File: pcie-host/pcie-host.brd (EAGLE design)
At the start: 167.6 x 111.2 mm, 237 parts, among them Q1 BSH103, Q2 BSH103, Q3 NDS351AN, Q4 NDS351AN, Q5 NDS351AN, U100 UEI15-050-Q12P-C, U104 ISO7240M, U105 ISO7240M, U106 ISO7240M, U107 ISO7240M

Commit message: Initial PCIe host layout complete.
- Needs verification before fabrication.
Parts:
- removed 10K, 30.1K: 9.53k, jonnew:0603
- removed 13.3K: 30.1k, jonnew:0603
- removed C41: 100uF, jonnew:153CLV-0807
- removed C43: 22uF, jonnew:1210-POL
- removed C71: 0.1uF, jonnew:0402
- removed C99: 100nF, RHD2000_eval_board:0603
- removed DI0, DO0: SMA002, jonnew:SMA_JACK_CONREVSMA002-G
- removed TP15: +5V0, jonnew:TESTPOINT_0.035IN
- removed TP_DI0, TP_DI1: MISO1, jonnew:TP09SQ
- removed U$14: FMC_LPC_160_PIN, jonnew:FMC_LPC_MALE_WITH_SP601_BSILK
- removed U$15, U$8: SCREW4, jonnew:SCREW4
- added DI2, DO2: SMA002, jonnew:SMA_JACK_CONREVSMA002-G
- added FMC_LPC: FMC_LPC_160_PIN, jonnew:FMC_LPC_MALE_WITH_SP601_BSILK
- added R13: 4.7k, cyclops:0603
- added R29: 100, jonnew:0603
- added R37: 22, jonnew:0402
- added TP11: +3.3V, jonnew:TESTPOINT_0.035IN
- added TP12: +12V(FPGA), jonnew:TESTPOINT_0.035IN
- added TP5: PASS, jonnew:TP06R
- added TP9: VPROTECT(+4.3V), jonnew:TESTPOINT_0.035IN
- added U1: ISO, jonnew:SCREW4
- added U18: COMM, jonnew:SCREW4
- C1: value 0.1uF -> 1uF
- C10: value (none) -> 10nF
- C11: value (none) -> 0.01uF
- C12: value (none) -> 47nF
- C13: value 0.1uF -> 4.7uF; device jonnew:0603 -> jonnew:0805
- C14: value 10uF -> 0.1uF; device jonnew:1206 -> jonnew:0402
- C15, C16, C35: device RHD2000_eval_board:0603 -> jonnew:0402
- C17, C5, C55: device RHD2000_eval_board:0603 -> jonnew:0603
- C18: value 0.1uF -> 4.7uF; device RHD2000_eval_board:0603 -> jonnew:1206
- C19: value 22uF -> 4.7F; device jonnew:1210-POL -> jonnew:1206
- C20: value (none) -> 1uF; device jonnew:0402 -> jonnew:0805
- C21, C24: value (none) -> 22uF; device jonnew:0402 -> jonnew:1206
- C22: value (none) -> 4.7uF; device jonnew:0402 -> jonnew:1206
- C23: value (none) -> 0.1uF
- C25: value 100nF -> 0.1uF; device jonnew:0603 -> RHD2000_eval_board:0603
- C26: value 1uF -> 0.01uF; device RHD2000_eval_board:0603 -> jonnew:0402
- C27: value 22uF -> 10nF; device jonnew:1210-POL -> jonnew:0402
- C28: value 4.7uF -> 10nF; device jonnew:0805 -> jonnew:0402
- C29: value 100nF -> 0.1uF; device jonnew:0603 -> jonnew:0402
- C3: value 10uF -> 4.7uF; device jonnew:1206 -> jonnew:0805
- C30, C32, C33: value 0.1uF -> 10nF; device jonnew:0603 -> jonnew:0402
- C31: value 100nF -> 10nF; device jonnew:0603 -> jonnew:0402
- C34, C36, C37: device jonnew:0603 -> jonnew:0402
- C38: value 0.01uF -> 4.7uF; device jonnew:0402 -> jonnew:1206
- C39, C59: value 22uF -> 0.1uF; device jonnew:1206 -> jonnew:0603
- C4: value 0.1uF -> 10uF; device RHD2000_eval_board:0603 -> jonnew:0603
- C40: value 100uF -> 0.1uF; device jonnew:153CLV-0807 -> jonnew:0603
- C42: value 22uF -> 10uF; device jonnew:1210-POL -> jonnew:1206
- C44: value (none) -> 100uF; device jonnew:0402 -> jonnew:153CLV-0807
- C45: value (none) -> 10uF; device jonnew:0402 -> jonnew:1206
- C46: value (none) -> 47uF; device jonnew:0402 -> jonnew:153CLV-0807
- C47, C48: value (none) -> 22uF; device jonnew:0402 -> jonnew:1210-POL
- C49, C7, C95: value 22uF -> 0.1uF; device jonnew:1210-POL -> jonnew:0603
- C50, C8, C9: value (none) -> 0.1uF; device jonnew:0402 -> jonnew:0603
- C51, C53, C61: value 1nF -> 0.1uF; device jonnew:0402 -> jonnew:0603
- C52, C56, C93, C97: value 100nF -> 0.1uF; device RHD2000_eval_board:0603 -> jonnew:0603
- C54: value 1uF -> 0.1uF; device jonnew:0805 -> jonnew:0603
- C57, C58, C91: value 100nF -> 0.1uF
- C60, C81: value 0.01uF -> 0.1uF; device jonnew:0402 -> jonnew:0603
- C62, C64: value 100nF -> (none); device RHD2000_eval_board:0603 -> jonnew:0402
- C63, C65: value 1nF -> (none)
- C66: value 47uF -> 22uF
- C67, C69, C73, C76, C79: value 0.1uF -> (none)
- C68, C70, C72, C75, C78: value 0.01uF -> (none)
- C74: value 4.7uF -> (none); device jonnew:1206 -> jonnew:0402
- C77: value 4.7F -> (none); device jonnew:1206 -> jonnew:0402
- C80, C84: value 4.7uF -> 0.1uF; device jonnew:1206 -> jonnew:0603
- C82: device jonnew:0402 -> jonnew:0603
- C83: value 0.01uF -> 1nF
- C85, C89: value 0.1uF -> 1nF
- C86: value 4.7uF -> 0.1uF; device jonnew:0805 -> jonnew:0603
- C87: value 0.1uF -> 22uF; device jonnew:0603 -> jonnew:1210-POL
- C88: value 0.047uF -> 0.1uF; device jonnew:0402 -> jonnew:0603
- C90, C94: value 100nF -> 1nF; device RHD2000_eval_board:0603 -> jonnew:0402
- C92: value 10uF -> 0.1uF
- L7/0R: value 1uH -> 74438356010
- Q1, Q2: value BSH103 -> NDS351AN
- Q3, Q4: value NDS351AN -> BSH103
- R1, R2: value 150, 0.25W -> 220; device jonnew:1206 -> cyclops:0603
- R10, R5: value 1k -> 2.2k
- R11: value 2.2k -> 820; device jonnew:0603 -> RHD2000_eval_board:0603
- R12: value 100 -> 4.7k; device jonnew:0603 -> cyclops:0603
- R14, R25: value 2.2k -> 10K; device jonnew:0603 -> jonnew:0402
- R15: value 100 -> 10K; device jonnew:0603 -> jonnew:0402
- R16, R23: value 10k -> 150, 0.25W; device jonnew:0603 -> jonnew:1206
- R18, R19: value 150, 0.25W -> 10K; device jonnew:1206 -> jonnew:0402
- R20: value 2.2k -> 1K
- R21, R24: value 2.2k -> 150, 0.25W; device jonnew:0603 -> jonnew:1206
- R22: value 100 -> 150, 0.25W; device jonnew:0603 -> jonnew:1206
- R26, R27: value 2.2k -> 10k
- R28: value 9.53k -> 100
- R3: value 150, 0.25W -> 100k; device jonnew:1206 -> cyclops:0603
- R30: value 1K -> 49.9; device jonnew:0603 -> jonnew:0402
- R31: value 1K -> 2.2k
- R32: value 49.9 -> 2.2k; device jonnew:0402 -> jonnew:0603
- R33: value 220 -> 1k
- R34: value 1k -> 100k
- R35: value 220 -> 22; device cyclops:0603 -> jonnew:0402
- R36: value 4.7k -> 22; device cyclops:0603 -> jonnew:0402
- R38, R39, R40, R41, R42, R43, R44, R45: value 10K -> 22
- R4: value 1k -> 100k; device jonnew:0603 -> cyclops:0603
- R46: value 0 -> 220; device jonnew:0402 -> cyclops:0603
- R47, R48: value 0 -> 22
- R55: value 22 -> 30.1k; device jonnew:0402 -> jonnew:0603
- R56: value 22 -> 10k; device jonnew:0402 -> jonnew:0603
- R57, R60, R62: value 22 -> 10K
- R58, R61, R63: value 22 -> 0
- R59: value 22 -> 13.3k; device jonnew:0402 -> jonnew:0603
- R6, R8: value 820 -> 2.2k; device RHD2000_eval_board:0603 -> jonnew:0603
- R64: value 22 -> 649k; device jonnew:0402 -> jonnew:0603
- R65, R66: value 22 -> 1k; device jonnew:0402 -> jonnew:0603
- R67: value 22 -> 100; device jonnew:0402 -> jonnew:0603
- R68: value 100k -> 9.53k; device cyclops:0603 -> jonnew:0603
- R69: value 220 -> 2.2k; device cyclops:0603 -> jonnew:0603
- R7: value 649k -> 1K
- R70: value 4.7k -> 2.2k; device cyclops:0603 -> jonnew:0603
- R71, R72: value 100k -> 1k; device cyclops:0603 -> jonnew:0603
- R9: value 1k -> 820; device jonnew:0603 -> RHD2000_eval_board:0603
- TP1, TP10: value +3V6 -> GND
- TP13: value +3V3 -> +12V(ATX)
- TP2: value +3V6 -> +1.8V ISO; device jonnew:TP06R -> jonnew:TESTPOINT_0.035IN
- TP3: value (none) -> +3.3V(ISO)
- TP4: value (none) -> +12V(ISO)
- TP6: value (none) -> DI1; device jonnew:TESTPOINT_0.035IN -> jonnew:TP09SQ
- TP7: value (none) -> DI0; device jonnew:TESTPOINT_0.035IN -> jonnew:TP09SQ
- TP8: value +5V0 -> GND
- U11: value (none) -> ISO1541DR
- U12: value UEI15-050-Q12P-C -> S24SE12002
- U20: value SN65LVDS387_TSSOP -> SN65LVDS387
- moved TP13 132.5 mm to (132.0, 54.0), turned to 0 degrees
- moved TP7 131.2 mm to (32.7, 80.9)
- moved R5 130.8 mm to (13.9, 79.4), flipped to the top
- moved C87 126.7 mm to (103.6, 102.9), flipped to the bottom, turned to 0 degrees
- moved TP6 126.0 mm to (32.7, 70.8)
- moved R68 113.9 mm to (114.8, 24.1), turned to 270 degrees
- moved R28 102.6 mm to (27.7, 78.4), turned to 0 degrees
- moved R9 98.4 mm to (17.3, 86.3), turned to 270 degrees
- moved R4 94.3 mm to (17.9, 60.9), turned to 180 degrees
- moved C3 93.9 mm to (9.50, 15.8), turned to 0 degrees
- moved C46 93.6 mm to (150.0, 33.0), turned to 0 degrees
- moved R7 92.3 mm to (10.5, 25.1)
- moved C80 89.8 mm to (109.8, 97.0), turned to 90 degrees
- moved R71 88.4 mm to (105.5, 49.2)
- moved R10 88.2 mm to (25.2, 81.3), turned to 270 degrees
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- renumbered D9 to D6, L7 to L7/0R, U$1 to U11, U$10 to U8, U$11 to U19, U$12 to U17, U$13 to U21, U$17 to U3, U$18 to U2, U$2 to X1, U$21 to U7, U$3 to U10, U$4 to U20, U$5 to U5, U$6 to U6, U$7 to U4, U$9 to U9, U100 to U12, U104 to U16, U105 to U15, U106 to U14, U107 to U13, USER to OUT
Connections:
- removed net DO_N: U$14.P$98, U20.63
- removed net DO_P: U$14.P$97, U20.64
- removed net N$134: U$15.P$2
- removed net N$14 (its old number): DO0.CLK, F1.1
- removed net N$147: R35.2
- new net D0_N: FMC_LPC.P$98, U20.63
- new net D0_P: FMC_LPC.P$97, U20.64
- new net N$17: DO2.CLK, F4.1
- net $N1: now also D4.3, F2.2, R22.2, R24.2, R29.1, R6.2; no longer D2.3, F4.2, R18.2, R19.2, R20.2, R22.1
- net $N101: now also D1.3, F3.2, R13.2; no longer D3.3, F1.2, R36.2
- net $N2: now also D2.3, F4.2, R12.2; no longer D4.3, F3.2, R70.2
- net $N3: now also D3.3, F1.2, R16.2, R21.2, R23.2, R28.1, R5.2; no longer D1.3, F2.2, R1.2, R11.2, R15.1, R2.2, R3.2
- net +12V_ATX: now also C44.+, C46.+, TP13.1; no longer C40.+, C41.+, C42.+, C43.+, C66.+, TP7.1, U$8.P$4
- net +12V_FPGA: now also C66.+, C80.2, C82.2, FMC_LPC.P$155, FMC_LPC.P$157, R69.2, R70.2, TP12.1, U18.P$3; no longer C49.+, C7.+, C91.2, R26.2, R27.2, TP6.1, U$14.P$155, U$14.P$157, U$8.P$3
- net +12V_ISO: now also C13.2, C17.1, C42.2, C45.2, C47.+, C48.+, TP4.1; no longer C14.2, C19.+, C28.2, C3.2, C30.1, C95.+, TP15.1
- net +1V8_ISO: now also C24.2, C31.2, C32.2, C33.2, C35.2, C36.2, C37.2, R57.1, R60.1, R62.1, TP2.1, U1.P$2; no longer C38.2, C59.2, C67.2, C68.2, C69.2, C70.2, C71.2, R43.1, R44.1, R45.1, TP10.1
- net +3V3: now also C2.2, C20.2, C58.2, C59.2, C60.2, C8.1, C81.2, C83.2, C84.2, C85.2, C86.2, C87.+, C88.2, C89.2, C9.1, C91.2, C92.2, C94.2, C95.2, FMC_LPC.P$116, FMC_LPC.P$118, FMC_LPC.P$120, FMC_LPC.P$159, R1.2, R11.1, R2.2, R31.2, R32.2, R67.2, R71.2, R72.2, R9.1, TP11.1, U18.P$2; no longer C17.2, C18.2, C26.2, C27.+, C29.2, C31.2, C35.2, C36.1, C37.1, C4.2, C51.2, C52.2, C53.2, C54.2, C55.2, C62.2, C63.2, C64.2, C65.2, C99.2, R12.2, R24.2, R25.2, R4.2, R5.2, R6.1, R69.2, R8.1, TP4.1, U$14.P$116, U$14.P$118, U$14.P$120, U$14.P$159, U$8.P$2
- net +3V3_ISO: now also C21.2, C27.2, C28.2, C29.2, C30.2, C34.2, C38.2, C49.2, C50.2, C51.2, C52.2, C53.2, C54.2, R14.2, R15.2, R18.2, R19.2, R25.1, R46.2, R65.2, R66.2, TP3.1, U1.P$3; no longer C15.2, C16.2, C2.2, C39.2, C5.2, C58.2, C60.2, C81.2, C82.2, C83.2, C84.2, C85.2, C94.2, R10.2, R33.2, R38.2, R39.2, R40.2, R41.2, R42.1, R9.2, TP13.1, U$15.P$3
- net +3V3_ISO_PG: now also C79.1; no longer C50.1
- net +3V3_ISO_PG_ISO: now also R56.2; no longer 10K.2
- net +3V3_ISO_PG_N: now also FMC_LPC.P$89; no longer U$14.P$89
- net +3V3_ISO_PG_P: now also FMC_LPC.P$88; no longer U$14.P$88
- net 2V5_REF: now also R67.1; no longer R12.1
- net BISTEN: now also R19.1; no longer R41.1
- net D0: now also C76.1; no longer C48.1
- net D0_ISO: now also R54.1; no longer R58.1
- net D1: now also C72.1; no longer C47.1
- net D10: now also C69.1; no longer C12.1
- net D10_ISO: now also R35.1; no longer R59.1
- net D10_N: now also FMC_LPC.P$50; no longer U$14.P$50
- net D10_P: now also FMC_LPC.P$49; no longer U$14.P$49
- net D11: now also C64.1; no longer C11.1
- net D11_ISO: now also R42.1; no longer R60.1
- net D11_N: now also FMC_LPC.P$8; no longer U$14.P$8
- net D11_P: now also FMC_LPC.P$7; no longer U$14.P$7
- net D1_ISO: now also R38.1; no longer R57.1
- net D1_N: now also FMC_LPC.P$17; no longer U$14.P$56
- net D1_P: now also FMC_LPC.P$16; no longer U$14.P$55
- net D2: now also C67.1; no longer C46.1
- net D2_ISO: now also R45.1; no longer R56.1
- net D2_N: now also FMC_LPC.P$56; no longer U$14.P$17
- net D2_P: now also FMC_LPC.P$55; no longer U$14.P$16
- net D3: now also C62.1; no longer C45.1
- net D3_ISO: now also R53.1; no longer R55.1
- net D3_N: now also FMC_LPC.P$135; no longer U$14.P$135
- net D3_P: now also FMC_LPC.P$134; no longer U$14.P$134
- net D4: now also C77.1; no longer C44.1
- net D4_ISO: now also R37.1; no longer R54.1
- net D4_N: now also FMC_LPC.P$95; no longer U$14.P$95
- net D4_P: now also FMC_LPC.P$94; no longer U$14.P$94
- net D5: now also C73.1; no longer C24.1
- net D5_ISO: now also R44.1; no longer R53.1
- net D5_N: now also FMC_LPC.P$14; no longer U$14.P$53
- net D5_P: now also FMC_LPC.P$13; no longer U$14.P$52
- net D6: now also C68.1; no longer C23.1
- net D6_N: now also FMC_LPC.P$53; no longer U$14.P$14
- net D6_P: now also FMC_LPC.P$52; no longer U$14.P$13
- net D7: now also C63.1; no longer C22.1
- net D7_ISO: now also R36.1; no longer R51.1
- net D7_N: now also FMC_LPC.P$92; no longer U$14.P$92
- net D7_P: now also FMC_LPC.P$91; no longer U$14.P$91
- net D8: now also C78.1; no longer C21.1
- net D8_ISO: now also R43.1; no longer R50.1
- net D8_N: now also FMC_LPC.P$11; no longer U$14.P$131
- net D8_P: now also FMC_LPC.P$10; no longer U$14.P$130
- net D9: now also C74.1; no longer C20.1
- net D9_ISO: now also R51.1; no longer R49.1
- net D9_N: now also FMC_LPC.P$131; no longer U$14.P$11
- net D9_P: now also FMC_LPC.P$130; no longer U$14.P$10
- net DAC_LAT_N: now also FMC_LPC.P$20; no longer U$14.P$59
- net DAC_LAT_P: now also FMC_LPC.P$19; no longer U$14.P$58
- net DI0: now also TP7.TP; no longer TP_DI0.TP
- net DI0_N: now also FMC_LPC.P$68; no longer U$14.P$68
- net DI0_P: now also FMC_LPC.P$67; no longer U$14.P$67
- net DI0_TERM: now also Q3.G, R10.2; no longer Q1.G, R14.2
- net DI0_TERM_N: now also FMC_LPC.P$139; no longer U$14.P$139
- net DI0_TERM_P: now also FMC_LPC.P$138; no longer U$14.P$138
- net DI1: now also TP6.TP; no longer TP_DI1.TP
- net DI1_N: now also FMC_LPC.P$29; no longer U$14.P$29
- net DI1_P: now also FMC_LPC.P$28; no longer U$14.P$28
- net DI1_TERM: now also Q4.G, R8.2; no longer Q2.G, R21.2
- net DI1_TERM_N: now also FMC_LPC.P$59; no longer U$14.P$20
- net DI1_TERM_P: now also FMC_LPC.P$58; no longer U$14.P$19
- net DO0_N: now also FMC_LPC.P$143; no longer U$14.P$143
- net DO0_P: now also FMC_LPC.P$142; no longer U$14.P$142
- net DO1_N: now also FMC_LPC.P$62; no longer U$14.P$23
- net DO1_P: now also FMC_LPC.P$61; no longer U$14.P$22
- net DOUTP_F: now also C16.2, R7.2; no longer C89.2, R30.2
- net DO_TEST_N: now also FMC_LPC.P$101; no longer U$14.P$101
- net DO_TEST_P: now also FMC_LPC.P$100; no longer U$14.P$100
- net GND: now also C2.1, C20.1, C44.-, C46.-, C58.1, C59.1, C6.2, C60.1, C62.2, C63.2, C64.2, C65.2, C67.2, C68.2, C69.2, C7.2, C70.2, C72.2, C73.2, C74.2, C75.2, C76.2, C77.2, C78.2, C79.2, C80.1, C81.1, C82.1, C83.1, C84.1, C85.1, C86.1, C87.-, C88.1, C89.1, C92.1, C94.1, C95.1, DI2.GND$1, DI2.GND$2, DI2.GND$3, DI2.GND$4, DO2.GND$1, DO2.GND$2, DO2.GND$3, DO2.GND$4, FMC_LPC.GNDA, FMC_LPC.GNDB, FMC_LPC.P$102, FMC_LPC.P$105, FMC_LPC.P$108, FMC_LPC.P$117, FMC_LPC.P$119, FMC_LPC.P$12, FMC_LPC.P$121, FMC_LPC.P$124, FMC_LPC.P$125, FMC_LPC.P$128, FMC_LPC.P$129, FMC_LPC.P$132, FMC_LPC.P$133, FMC_LPC.P$136, FMC_LPC.P$137, FMC_LPC.P$140, FMC_LPC.P$141, FMC_LPC.P$144, FMC_LPC.P$145, FMC_LPC.P$148, FMC_LPC.P$149, FMC_LPC.P$15, FMC_LPC.P$152, FMC_LPC.P$153, FMC_LPC.P$156, FMC_LPC.P$158, FMC_LPC.P$160, FMC_LPC.P$18, FMC_LPC.P$21, FMC_LPC.P$24, FMC_LPC.P$27, FMC_LPC.P$3, FMC_LPC.P$30, FMC_LPC.P$33, FMC_LPC.P$36, FMC_LPC.P$39, FMC_LPC.P$41, FMC_LPC.P$44, FMC_LPC.P$45, FMC_LPC.P$48, FMC_LPC.P$51, FMC_LPC.P$54, FMC_LPC.P$57, FMC_LPC.P$6, FMC_LPC.P$60, FMC_LPC.P$63, FMC_LPC.P$66, FMC_LPC.P$69, FMC_LPC.P$72, FMC_LPC.P$75, FMC_LPC.P$78, FMC_LPC.P$80, FMC_LPC.P$82, FMC_LPC.P$83, FMC_LPC.P$86, FMC_LPC.P$87, FMC_LPC.P$9, FMC_LPC.P$90, FMC_LPC.P$93, FMC_LPC.P$96, FMC_LPC.P$99, R10.1, R3.1, R4.1, R5.1, R6.1, R8.1, TP10.1, TP8.1, U18.P$1, U18.P$4; no longer C10.2, C11.2, C12.2, C17.1, C18.1, C20.2, C21.2, C22.2, C23.2, C24.2, C26.1, C27.-, C29.1, C31.1, C33.2, C34.2, C35.1, C36.2, C37.2, C4.1, C40.-, C41.-, C42.-, C43.-, C44.2, C45.2, C46.2, C47.2, C48.2, C49.-, C50.2, C51.1, C52.1, C53.1, C54.1, C6.1, C62.1, C63.1, C64.1, C65.1, C7.-, C99.1, DI0.GND$1, DI0.GND$2, DI0.GND$3, DI0.GND$4, DO0.GND$1, DO0.GND$2, DO0.GND$3, DO0.GND$4, R11.1, R14.1, R20.1, R21.1, R68.1, R71.1, TP3.1, U$14.GNDA, U$14.GNDB, U$14.P$102, U$14.P$105, U$14.P$108, U$14.P$117, U$14.P$119, U$14.P$12, U$14.P$121, U$14.P$124, U$14.P$125, U$14.P$128, U$14.P$129, U$14.P$132, U$14.P$133, U$14.P$136, U$14.P$137, U$14.P$140, U$14.P$141, U$14.P$144, U$14.P$145, U$14.P$148, U$14.P$149, U$14.P$15, U$14.P$156, U$14.P$158, U$14.P$160, U$14.P$18, U$14.P$21, U$14.P$24, U$14.P$27, U$14.P$3, U$14.P$30, U$14.P$33, U$14.P$36, U$14.P$39, U$14.P$41, U$14.P$44, U$14.P$45, U$14.P$48, U$14.P$51, U$14.P$54, U$14.P$57, U$14.P$6, U$14.P$60, U$14.P$63, U$14.P$66, U$14.P$69, U$14.P$72, U$14.P$75, U$14.P$78, U$14.P$80, U$14.P$82, U$14.P$83, U$14.P$86, U$14.P$87, U$14.P$9, U$14.P$90, U$14.P$93, U$14.P$96, U$14.P$99, U$8.P$1
- net GND_ISO: now also C10.1, C11.1, C17.2, C18.1, C19.1, C21.1, C22.1, C23.1, C24.1, C26.1, C27.1, C29.1, C30.1, C31.1, C33.1, C34.1, C35.1, C36.1, C37.1, C4.1, C40.1, C42.1, C45.1, C47.-, C48.-, C49.1, C5.2, C50.1, C51.1, C52.1, C53.1, C54.1, R30.2, R34.1, R55.2, R58.2, R59.2, R61.2, R63.2, R64.2, R68.2, U1.P$1, U1.P$4; no longer 13.3K.2, 30.1K.2, C16.1, C19.-, C2.1, C30.2, C5.1, C58.1, C59.1, C60.1, C67.1, C68.1, C69.1, C70.1, C71.1, C72.1, C73.1, C74.1, C75.1, C76.1, C77.1, C78.1, C79.1, C80.1, C81.1, C82.1, C83.1, C84.1, C85.1, C86.1, C87.2, C92.1, C94.1, C95.-, R28.2, R32.2, R46.2, R47.2, R48.2, R7.2, R72.1, U$15.P$1, U$15.P$4
- net GPI0_ISO: now also R48.1; no longer R67.1
- net GPI0_N: now also FMC_LPC.P$26; no longer U$14.P$65
- net GPI0_P: now also FMC_LPC.P$25; no longer U$14.P$64
- net GPI1_ISO: now also R40.1; no longer R66.1
- net GPI1_N: now also FMC_LPC.P$104; no longer U$14.P$104
- net GPI1_P: now also FMC_LPC.P$103; no longer U$14.P$103
- net GPO0_ISO: now also R47.1; no longer R65.1
- net GPO0_N: now also FMC_LPC.P$23; no longer U$14.P$62
- net GPO0_P: now also FMC_LPC.P$22; no longer U$14.P$61
- net GPO1_ISO: now also R39.1; no longer R64.1
- net GPO1_N: now also FMC_LPC.P$65; no longer U$14.P$26
- net GPO1_P: now also FMC_LPC.P$64; no longer U$14.P$25
- net HSYNC: now also C65.1; no longer C8.1
- net HSYNC_ISO: now also R50.1; no longer R61.1
- net HSYNC_N: now also FMC_LPC.P$85; no longer U$14.P$85
- net HSYNC_P: now also FMC_LPC.P$84; no longer U$14.P$84
- net IDX0: now also R57.2, R58.1; no longer R43.2, R46.1
- net IDX1: now also R60.2, R61.1; no longer R44.2, R47.1
- net INTVCC: now also R56.1; no longer 10K.1
- net LOCK: now also R33.2; no longer R34.2
- net MODE: now also R62.2, R63.1; no longer R45.2, R48.1
- net N$1: now also TP5.TP; no longer TP2.TP
- net N$10: now also R55.1; no longer 30.1K.1
- net N$11: now also DI1.CLK, F1.1; no longer DI0.CLK, F2.1
- net N$12: now also C40.2; no longer C32.2
- net N$13: now also R41.2; no longer R62.2
- net N$136: now also R26.1; no longer R16.1
- net N$145: now also R64.1; no longer R7.1
- net N$15: now also R46.1; no longer R33.1
- net N$16: now also R50.2; no longer R61.2
- net N$18: now also C6.1, R26.2; no longer C33.1, R16.2
- net N$19: now also R29.2; no longer R22.2
- net N$2: now also Q3.D, R16.1, R21.1, R23.1; no longer Q1.D, R1.1, R2.1, R3.1
- net N$20: now also C7.1, R27.2; no longer C34.1, R23.2
- net N$21: now also R20.2, R7.1; no longer R30.1, R31.2
- net N$22: now also C3.2, C5.1, R20.1; no longer C86.2, C87.1, R31.1
- net N$23: now also R1.1; no longer R35.1
- net N$24: now also R31.1; no longer R24.1
- net N$25: now also R32.1; no longer R25.1
- net N$26: now also R68.1; no longer R28.1
- net N$27: now also C16.1; no longer C89.1
- net N$28: now also C12.1; no longer C88.1
- net N$3: now also R28.2; no longer R15.2
- net N$30: now also R9.2; no longer R6.2
- net N$31: now also R2.1; no longer R69.1
- net N$32: now also C12.2, R30.1; no longer C88.2, R32.1
- net N$33: now also R11.2; no longer R8.2
- net N$35: now also Q1.D; no longer Q3.D
- net N$36: now also R27.1; no longer R23.1
- net N$39: now also Q1.G, R13.1, R3.2; no longer Q3.G, R36.1, R68.2
- net N$4: now also R49.2; no longer R63.2
- net N$44: now also R51.2; no longer R49.2
- net N$45: now also R43.2; no longer R50.2
- net N$46: now also R36.2; no longer R51.2
- net N$48: now also R44.2; no longer R53.2
- net N$49: now also R37.2; no longer R54.2
- net N$5: now also R59.1; no longer 13.3K.1
- net N$50: now also R53.2; no longer R55.2
- net N$51: now also R45.2; no longer R56.2
- net N$52: now also R38.2; no longer R57.2
- net N$53: now also R54.2; no longer R58.2
- net N$54: now also R42.2; no longer R60.2
- net N$55: now also R35.2; no longer R59.2
- net N$56: now also R39.2; no longer R64.2
- net N$57: now also R47.2; no longer R65.2
- net N$58: now also R40.2; no longer R66.2
- net N$59: now also R48.2; no longer R67.2
- net N$6: now also DI2.CLK, F2.1; no longer DI1.CLK, F4.1
- net N$60: now also Q2.D; no longer Q4.D
- net N$61: now also Q2.G, R12.1, R4.2; no longer Q4.G, R70.1, R71.2
- net N$62: now also R33.1, R34.2; no longer R34.1, R72.2
- net N$7: now also Q4.D, R22.1, R24.1; no longer Q2.D, R18.1, R19.1
- net N$8: now also C39.2; no longer C13.2
- net OEN: now also R15.1; no longer R40.1
- net OSS_SEL: now also R18.1; no longer R39.1
- net PCLK: now also C75.1; no longer C10.1
- net PCLK_ISO: now also R49.1; no longer R63.1
- net PCLK_N: now also FMC_LPC.P$43; no longer U$14.P$43
- net PCLK_P: now also FMC_LPC.P$42; no longer U$14.P$42
- net PDN: now also C4.2, R25.2; no longer C92.2, R42.2
- net SCL: now also FMC_LPC.P$150, R72.1; no longer R5.1, U$14.P$150
- net SCL_ISO: now also R65.1; no longer R10.1
- net SDA: now also FMC_LPC.P$151, R71.1; no longer R4.1, U$14.P$151
- net SDA_ISO: now also R66.1; no longer R9.1
- net SEL: now also R14.1; no longer R38.1
- net TDI-TDO: now also FMC_LPC.P$110, FMC_LPC.P$111; no longer U$14.P$110, U$14.P$111
- net VDDCML0: now also C11.2, C15.2, C19.2, L5.1; no longer C75.2, C76.2, C77.2, L4.1
- net VDDCML1: now also C10.2, C14.2, C18.2, L4.1; no longer C78.2, C79.2, C80.2, L5.1
- net VDDPLL: now also C22.2, C23.2, C26.2; no longer C72.2, C73.2, C74.2
- net VSYNC: now also C70.1; no longer C9.1
- net VSYNC_ISO: now also R41.1; no longer R62.1
- net VSYNC_N: now also FMC_LPC.P$5; no longer U$14.P$5
- net VSYNC_P: now also FMC_LPC.P$4; no longer U$14.P$4
- net V_PROTECT: now also C55.2, R69.1, R70.1, TP9.1; no longer C6.2, R26.1, R27.1, TP8.1
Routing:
- net SCL: track 0.00 -> 137.8 mm, vias 0 -> 4
- net SDA: track 0.00 -> 137.7 mm, vias 0 -> 3
- net +12V_FPGA: track 2.00 -> 120.2 mm, vias 0 -> 3
- net D0_P: track 0.00 -> 95.9 mm, vias 0 -> 2
- net D0_N: track 0.00 -> 95.8 mm, vias 0 -> 2
- net +3V3_ISO_PG_ISO: track 3.36 -> 90.4 mm, vias 0 -> 2
- net GND: track 130.5 -> 208.8 mm, vias 89 -> 170
- net DO_P: track 67.0 -> 0.00 mm
- net DO_N: track 66.3 -> 0.00 mm
- net +3V3: track 108.3 -> 148.0 mm, vias 34 -> 40
- net D3_P: track 61.9 -> 99.5 mm, vias 0 -> 2
- net D3_N: track 61.2 -> 98.7 mm, vias 0 -> 2
- net D4_N: track 59.5 -> 95.7 mm, vias 0 -> 2
- net D4_P: track 60.2 -> 95.9 mm
- net D2_N: track 62.9 -> 95.5 mm
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- added copper zone on layer 15, net +12V_ISO
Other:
- board text added: "+1.8V(ISO)"
- board text added: "+12V(FPGA)"
- board text added: "+2.5V"
- board text added: "+3,3V(ISO)"
- board text added: "+3.3V"
- board text added: "Deserializer/IO Board"
- board text added: "GND(ISO)"
- board text added: "INPUT LOGIC THRESHOLDS"
- board text added: "Rev. 1.0 CC BY-SA-NC-4.0 JPN, MWL@MIT 2017-04"
- board text added: "VBIAS0"
- board text added: "VBIAS1"
- board text removed: "+"
- board text removed: "+3v3"
- board text removed: "+3v6"
- board text removed: "-"
- board text removed: "A"
- board text removed: "B"
- board text removed: "C"
- board text removed: "COMMON"
- board text removed: "FMC IO Module Rev. 0.1 2016.03"
- board text removed: "FMC_12P0V"
- board text removed: "G21"
- board text removed: "G22"
- board text removed: "G24"
- board text removed: "VDD_AUX"
- board text removed: "direct FMC 3.3V ONLY"
- board text removed: "from FMC H23"
- board text removed: "isolated"
- board text removed: "to FMC H13"
- board text removed: "to FMC H14"

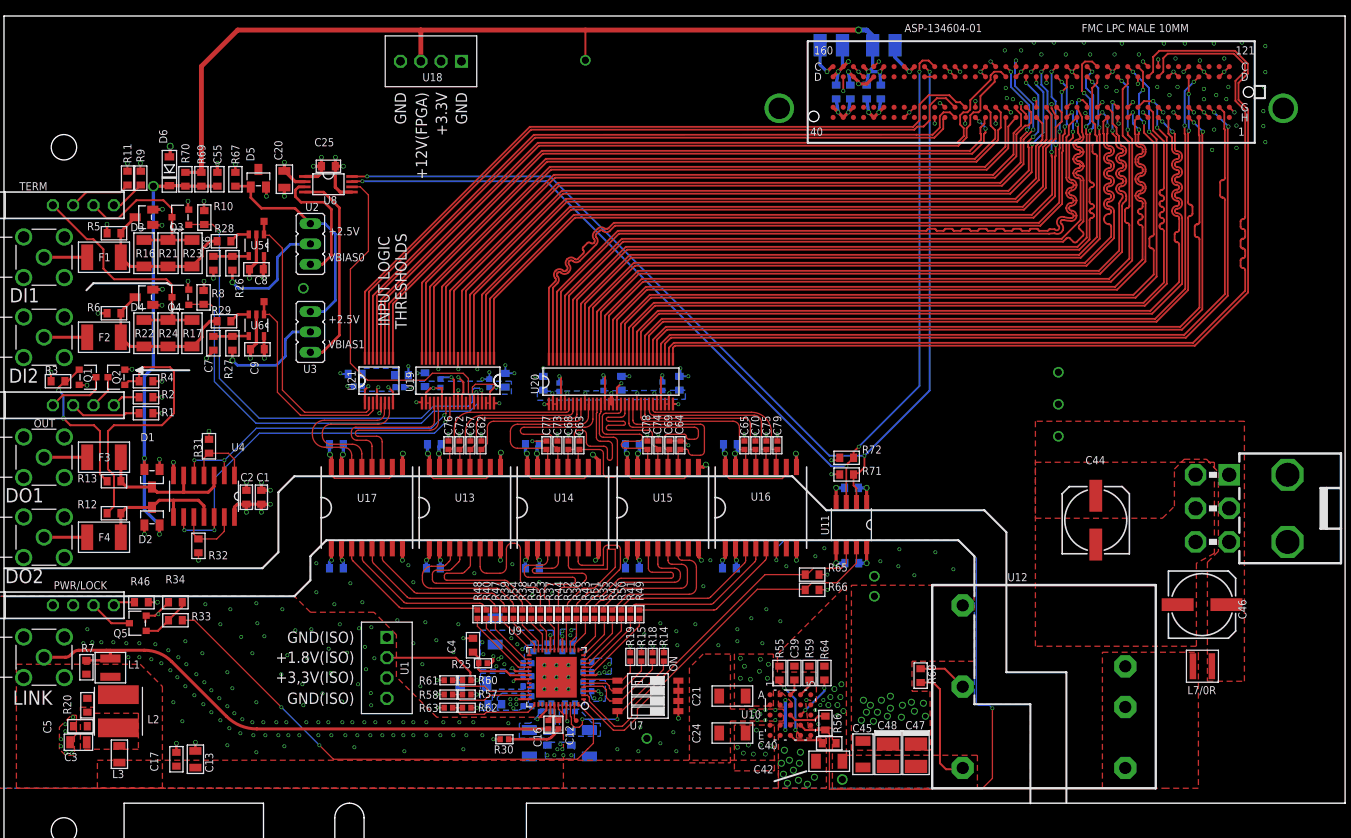
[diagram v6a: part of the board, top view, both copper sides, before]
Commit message: PCIe host board ready for fabrication
- Jack looked it over. Found a few minor things.
- Created gerbers.
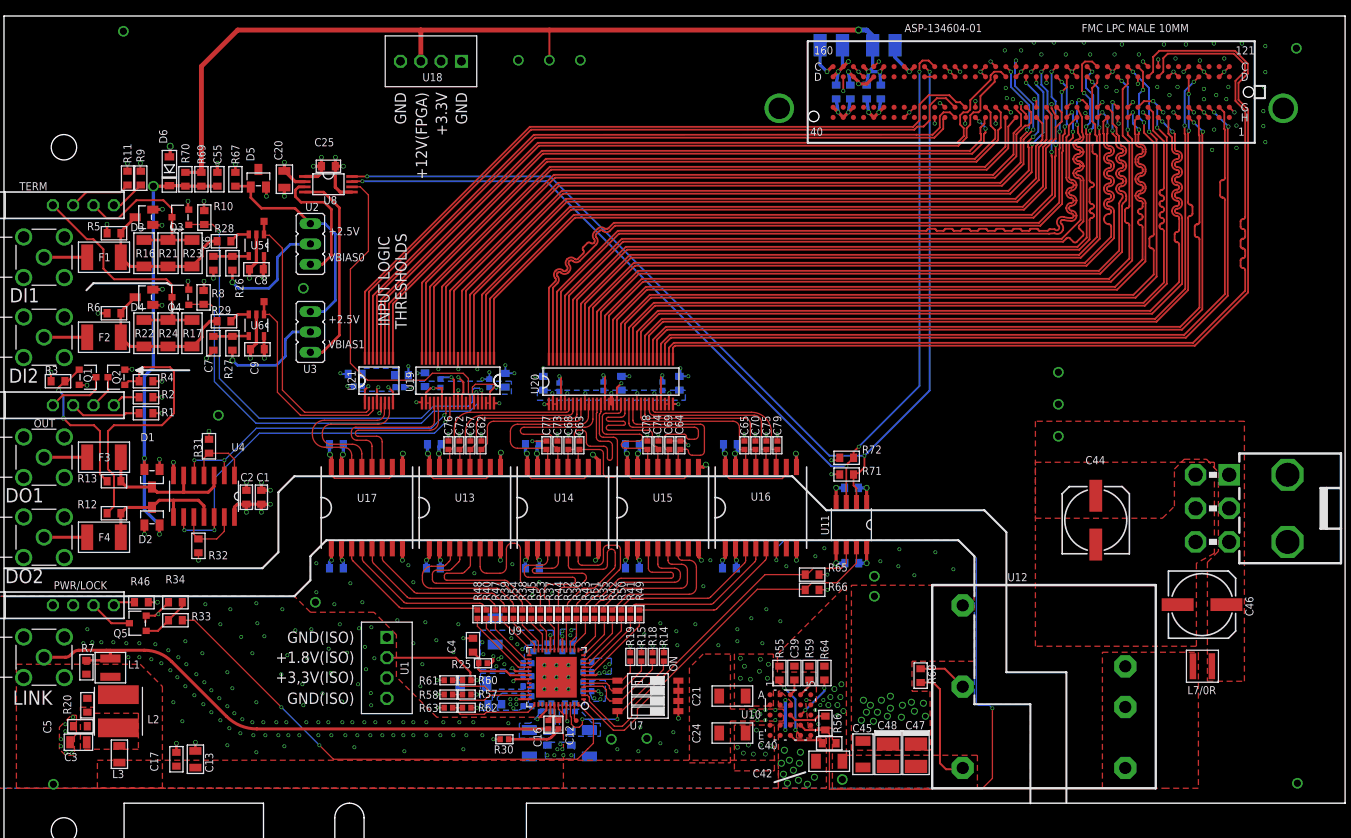
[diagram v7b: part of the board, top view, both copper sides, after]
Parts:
- added TP14, TP15, TP16, TP17, TP21: GND, jonnew:TESTPOINT_0.035IN
- added TP18, TP19, TP20: GND(ISO), jonnew:TESTPOINT_0.035IN
- added TP22: +3.3V, jonnew:TESTPOINT_0.035IN
- C11, C26: value 0.01uF -> 10nF
- TP1: value GND -> GND(ISO)
- TP2: value +1.8V ISO -> +1.8V(ISO)
- moved TP12 4.50 mm to (68.4, 101.0)
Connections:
- net +3V3: now also TP22.1
- net GND: now also TP14.1, TP15.1, TP16.1, TP17.1, TP21.1
- net GND_ISO: now also TP18.1, TP19.1, TP20.1
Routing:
- net D6_ISO: track 21.6 -> 20.8 mm

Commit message: Fixed mislabed GPIO lines on PCIe host board.
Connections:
- net GPI0_ISO: now also R40.1, U17.P4; no longer R48.1, U17.P3
- net GPI1_ISO: now also R48.1, U17.P3; no longer R40.1, U17.P4
- net GPO0_ISO: now also R39.1, U17.P6; no longer R47.1, U17.P5
- net GPO1_ISO: now also R47.1, U17.P5; no longer R39.1, U17.P6
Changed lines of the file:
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@@
 <?xml version="1.0" encoding="utf-8"?>
 <!DOCTYPE eagle SYSTEM "eagle.dtd">
-<eagle version="6.6.0">
+<eagle version="6.5.0">
 <drawing>
 <settings>
@@
 <wire x1="59.375" y1="30.25" x2="59.375" y2="31.2166" width="0.152" layer="1"/>
 </signal>
-<signal name="GPI1_ISO">
+<signal name="GPI0_ISO">
 <contactref element="U17" pad="P4"/>
 <contactref element="R40" pad="1"/>
@@
 <wire x1="44.93075" y1="39.9992125" x2="45" y2="39.9299625" width="0.152" layer="1"/>
 </signal>
-<signal name="GPI0_ISO">
-<contactref element="U17" pad="P3"/>
-<contactref element="R48" pad="1"/>
-<wire x1="59.375" y1="32.2834" x2="59.1584" y2="32.5" width="0.152" layer="1"/>
-<wire x1="59.1584" y1="32.5" x2="49.9483125" y2="32.5" width="0.152" layer="1"/>
-<wire x1="49.9483125" y1="32.5" x2="49.594759375" y2="32.646446875" width="0.152" layer="1" curve="-45"/>
-<wire x1="49.594759375" y1="32.646446875" x2="43.807196875" y2="38.434009375" width="0.152" layer="1"/>
-<wire x1="43.807196875" y1="38.434009375" x2="43.66075" y2="38.7875625" width="0.152" layer="1" curve="-45"/>
-<wire x1="43.66075" y1="39.9992125" x2="43.66075" y2="38.7875625" width="0.152" layer="1"/>
-</signal>
-<signal name="GPO1_ISO">
+<signal name="GPO0_ISO">
 <contactref element="U17" pad="P6"/>
 <contactref element="R39" pad="1"/>
@@
 <wire x1="14.9286875" y1="58.8768" x2="17.0850875" y2="58.8768" width="0.254" layer="1"/>
 </signal>
-<signal name="GPO0_ISO">
+<signal name="GPO1_ISO">
 <contactref element="U17" pad="P5"/>
 <contactref element="R47" pad="1"/>
@@
 <wire x1="119.714" y1="92.964" x2="120.1712" y2="92.5068" width="0.2286" layer="1"/>
 </signal>
+<signal name="GPI1_ISO">
+<contactref element="R48" pad="1"/>
+<contactref element="U17" pad="P3"/>
+<wire x1="59.1584" y1="32.5" x2="49.9483125" y2="32.5" width="0.152" layer="1"/>
+<wire x1="49.9483125" y1="32.5" x2="49.594759375" y2="32.646446875" width="0.152" layer="1" curve="-45"/>
+<wire x1="49.594759375" y1="32.646446875" x2="43.807196875" y2="38.434009375" width="0.152" layer="1"/>
+<wire x1="43.807196875" y1="38.434009375" x2="43.66075" y2="38.7875625" width="0.152" layer="1" curve="-45"/>
+<wire x1="43.66075" y1="39.9992125" x2="43.66075" y2="38.7875625" width="0.152" layer="1"/>
+<wire x1="59.1584" y1="32.5" x2="59.375" y2="32.2834" width="0" layer="19" extent="1-1"/>
+</signal>
 </signals>
